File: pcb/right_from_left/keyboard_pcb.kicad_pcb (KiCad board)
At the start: 2 copper layers, 138.8 x 89.9 mm, 48 parts, among them J1 TRRS, J2 Conn_01x04_Male, K0 KEYSW, K1 KEYSW, K10 KEYSW, K11 KEYSW, K12 KEYSW, K13 KEYSW, K14 KEYSW, K15 KEYSW, K2 KEYSW, K20 KEYSW, K21 KEYSW, K22 KEYSW, K23 KEYSW, K24 KEYSW, K25 KEYSW, K3 KEYSW, K30 KEYSW, K31 KEYSW, K32 KEYSW, K4 KEYSW, K5 KEYSW, U1 PCF8574, U2 Pico

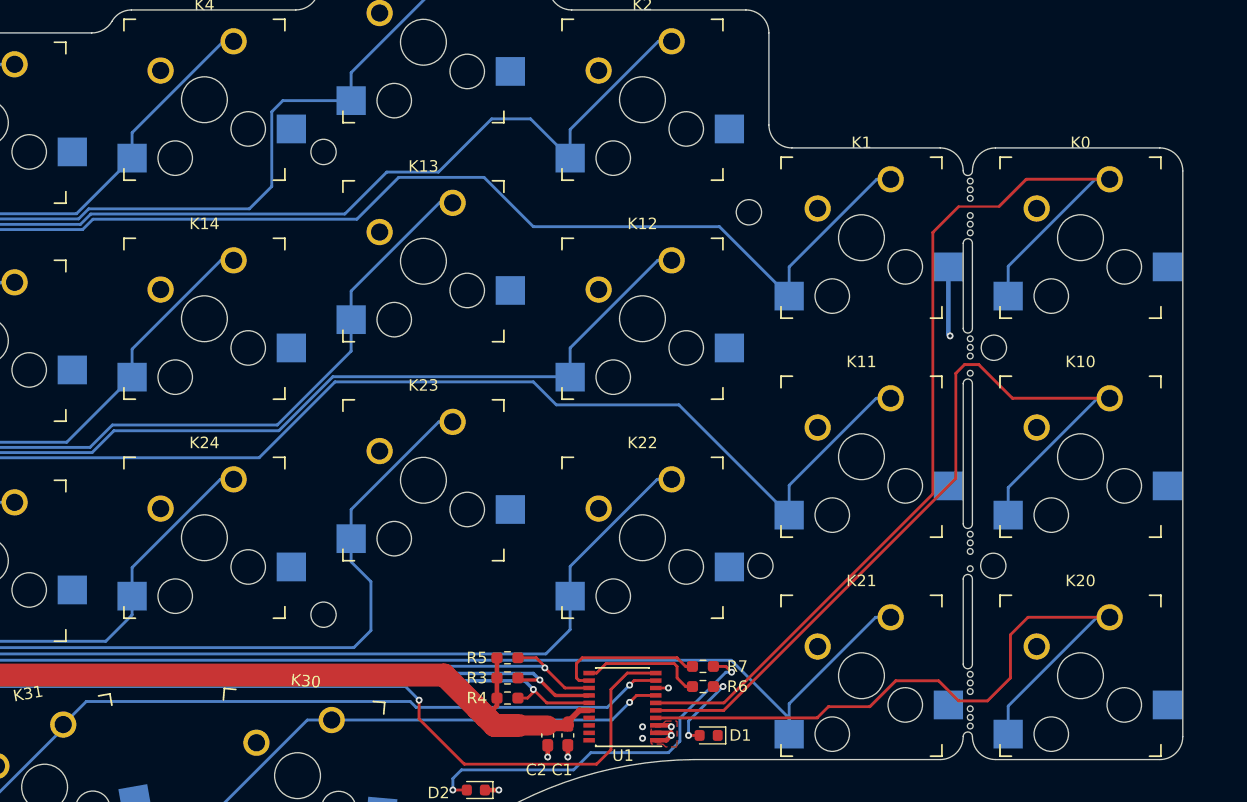
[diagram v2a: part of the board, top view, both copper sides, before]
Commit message: left keyboards routed
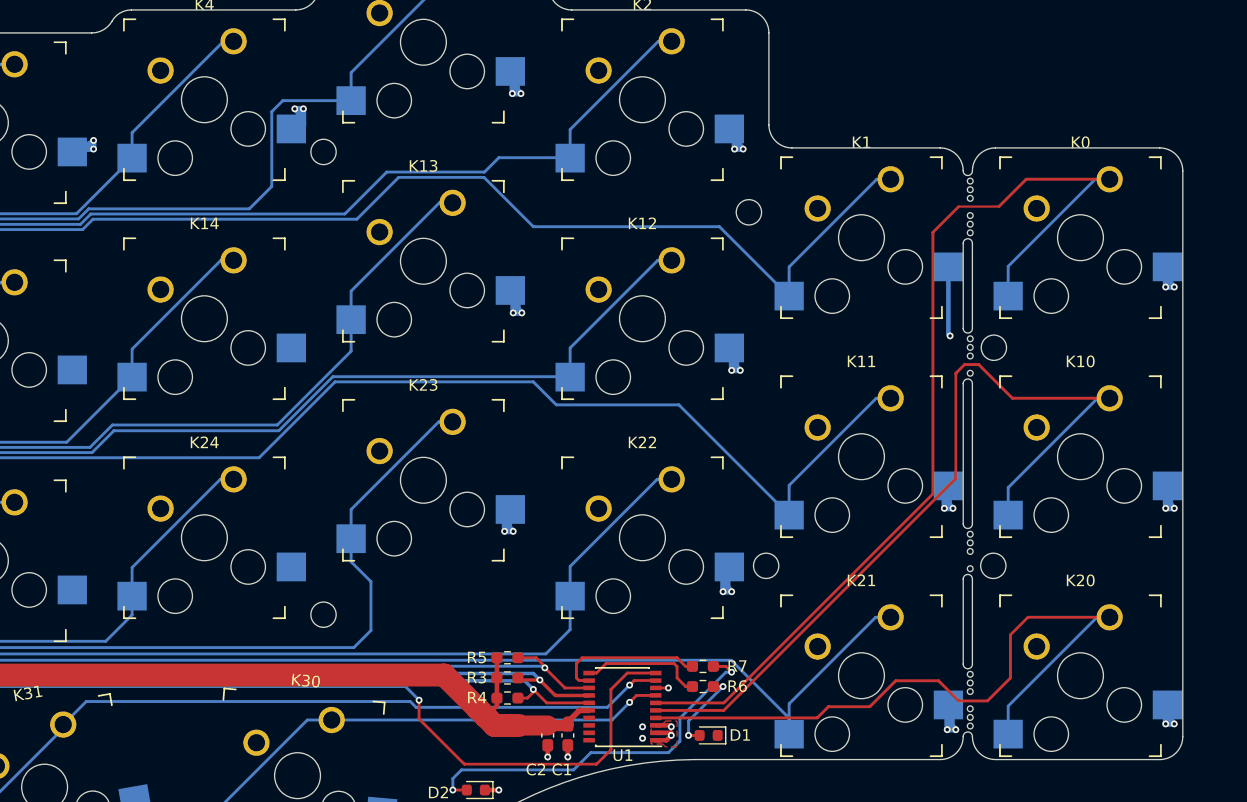
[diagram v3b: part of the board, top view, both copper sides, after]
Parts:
- moved H4 0.50 mm to (169.0, 96.8)
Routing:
- net GND: track 16.1 -> 71.6 mm, vias 10 -> 36
- net /k02: track 86.7 -> 83.9 mm
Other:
- board text added: "Right"

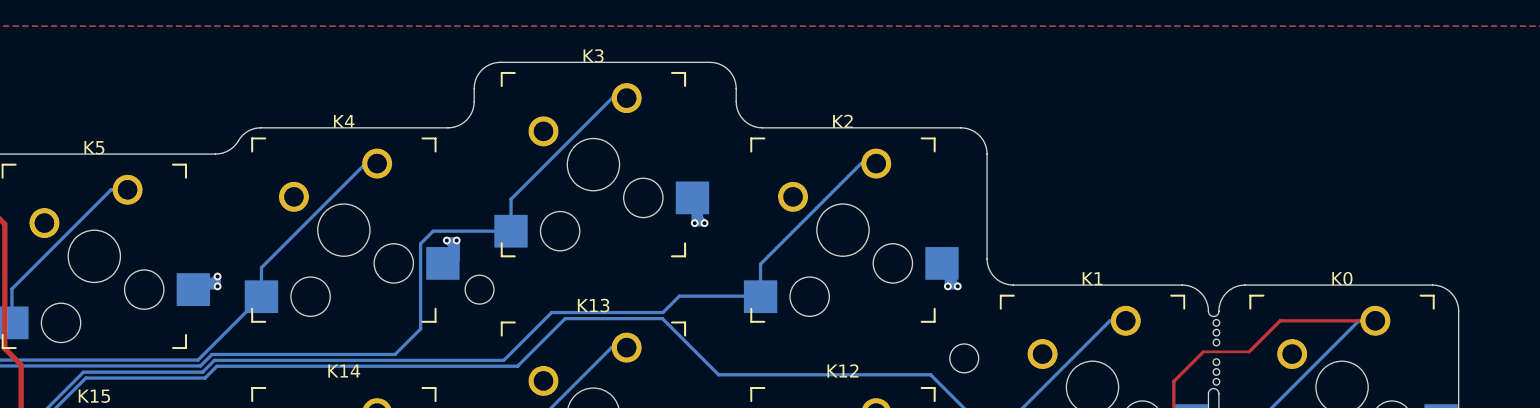
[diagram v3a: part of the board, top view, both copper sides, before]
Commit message: Left keyboard: Jumper to switch RX/TX direction removed in schematic and pcb.
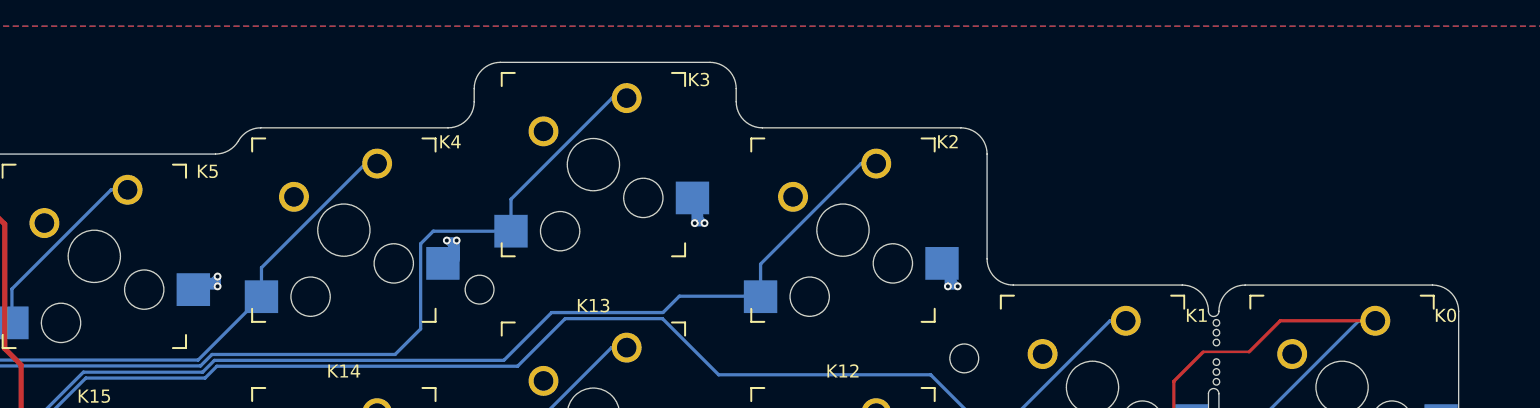
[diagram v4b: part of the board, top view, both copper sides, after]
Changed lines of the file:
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@@
         (effects (font (size 1 1) (thickness 0.15)))
     )
-    (fp_text value "KEYSW" (at 0 8.255) (layer "F.Fab")
+    (fp_text value "KEYSW" (at 4.46 -2.058) (layer "F.Fab")
         (effects (font (size 1 1) (thickness 0.15)))
     )
-    (fp_text user "${REFERENCE}" (at 3.81 8.255) (layer "B.SilkS")
+    (fp_text user "${REFERENCE}" (at 6.21 -7.558) (layer "B.SilkS")
         (effects (font (size 1 1) (thickness 0.15)) (justify mirror))
     )
-    (fp_text user "${VALUE}" (at 0 8.255) (layer "B.Fab")
+    (fp_text user "${VALUE}" (at 4.46 -2.058) (layer "B.Fab")
         (effects (font (size 1 1) (thickness 0.15)) (justify mirror))
     )
@@
     (property "Sheetname" "")
     (attr through_hole exclude_from_pos_files)
-    (fp_text reference "K2" (at 0 -8.255) (layer "F.SilkS")
+    (fp_text reference "K2" (at 8.01 -6.708) (layer "F.SilkS")
         (effects (font (size 1 1) (thickness 0.15)))
     )
@@
     (property "Sheetname" "")
     (attr through_hole exclude_from_pos_files)
-    (fp_text reference "K4" (at 0 -8.255) (layer "F.SilkS")
+    (fp_text reference "K4" (at 8.11 -6.708) (layer "F.SilkS")
         (effects (font (size 1 1) (thickness 0.15)))
     )
@@
         (effects (font (size 1 1) (thickness 0.15)))
     )
-    (fp_text value "KEYSW" (at 0 8.255 175) (layer "F.Fab")
+    (fp_text value "KEYSW" (at 9.974957 4.899268 175) (layer "F.Fab")
         (effects (font (size 1 1) (thickness 0.15)))
     )
@@
         (effects (font (size 1 1) (thickness 0.15)) (justify mirror))
     )
-    (fp_text user "${VALUE}" (at 0 8.255 175) (layer "B.Fab")
+    (fp_text user "${VALUE}" (at 9.974957 4.899268 175) (layer "B.Fab")
         (effects (font (size 1 1) (thickness 0.15)) (justify mirror))
     )
@@
     (property "Sheetname" "")
     (attr through_hole exclude_from_pos_files)
-    (fp_text reference "K1" (at 0 -8.255) (layer "F.SilkS")
+    (fp_text reference "K1" (at 7.96 -5.458) (layer "F.SilkS")
         (effects (font (size 1 1) (thickness 0.15)))
     )
@@
         (effects (font (size 1 1) (thickness 0.15)))
     )
-    (fp_text value "KEYSW" (at 0 8.255 25) (layer "F.Fab")
+    (fp_text value "KEYSW" (at 9.933865 7.114838 25) (layer "F.Fab")
         (effects (font (size 1 1) (thickness 0.15)))
     )
@@
         (effects (font (size 1 1) (thickness 0.15)) (justify mirror))
     )
-    (fp_text user "${VALUE}" (at 0 8.255 25) (layer "B.Fab")
+    (fp_text user "${VALUE}" (at 9.933865 7.114838 25) (layer "B.Fab")
         (effects (font (size 1 1) (thickness 0.15)) (justify mirror))
     )
@@
     (property "Sheetname" "")
     (attr through_hole)
-    (fp_text reference "K3" (at 0 -8.255) (layer "F.SilkS")
+    (fp_text reference "K3" (at 8.06 -6.458) (layer "F.SilkS")
         (effects (font (size 1 1) (thickness 0.15)))
     )
@@
     (property "Sheetname" "")
     (attr through_hole exclude_from_pos_files)
-    (fp_text reference "K5" (at 0 -8.255) (layer "F.SilkS")
+    (fp_text reference "K5" (at 8.66 -6.458) (layer "F.SilkS")
         (effects (font (size 1 1) (thickness 0.15)))
     )
@@
         (effects (font (size 1 1) (thickness 0.15)))
     )
-    (fp_text user "${REFERENCE}" (at 7.16 -1.558) (layer "B.SilkS")
+    (fp_text user "${REFERENCE}" (at 6.66 -8.308) (layer "B.SilkS")
         (effects (font (size 1 1) (thickness 0.15)) (justify mirror))
     )
@@
     (property "Sheetname" "")
     (attr through_hole exclude_from_pos_files)
-    (fp_text reference "K0" (at 0 -8.255) (layer "F.SilkS")
+    (fp_text reference "K0" (at 7.91 -5.458) (layer "F.SilkS")
         (effects (font (size 1 1) (thickness 0.15)))
     )
@@
         (effects (font (size 1 1) (thickness 0.15)))
     )
-    (fp_text value "KEYSW" (at 0 8.255 10) (layer "F.Fab")
+    (fp_text value "KEYSW" (at 9.988763 5.315282 10) (layer "F.Fab")
         (effects (font (size 1 1) (thickness 0.15)))
     )
@@
         (effects (font (size 1 1) (thickness 0.15)) (justify mirror))
     )
-    (fp_text user "${VALUE}" (at 0 8.255 10) (layer "B.Fab")
+    (fp_text user "${VALUE}" (at 9.988763 5.315282 10) (layer "B.Fab")
         (effects (font (size 1 1) (thickness 0.15)) (justify mirror))
     )

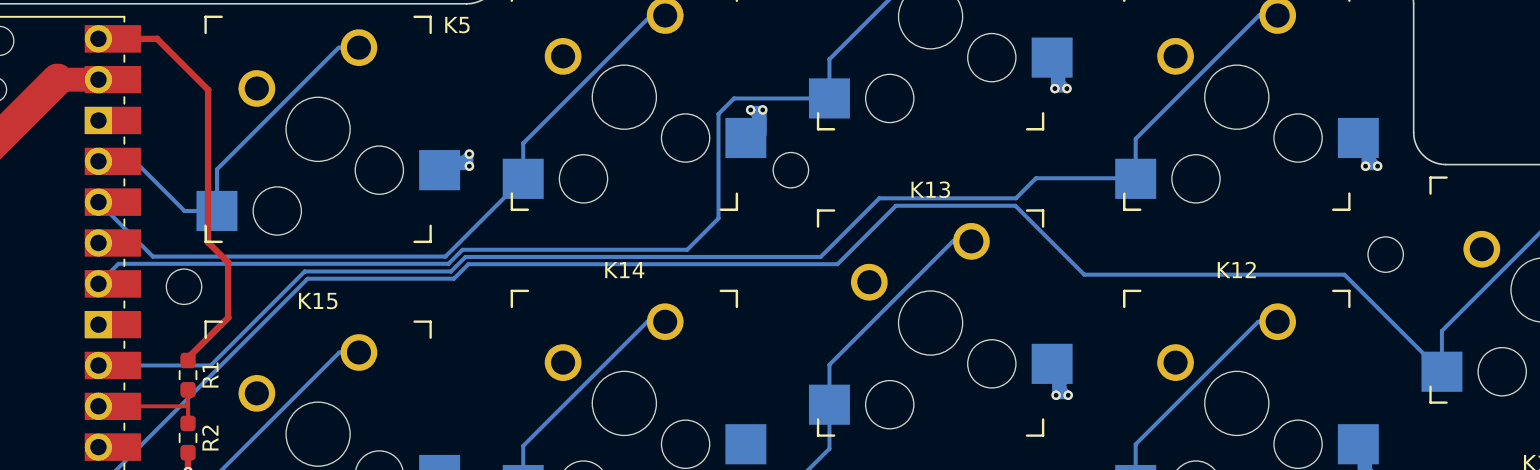
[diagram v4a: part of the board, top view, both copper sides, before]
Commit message: finetuning regarding BOM and part placement
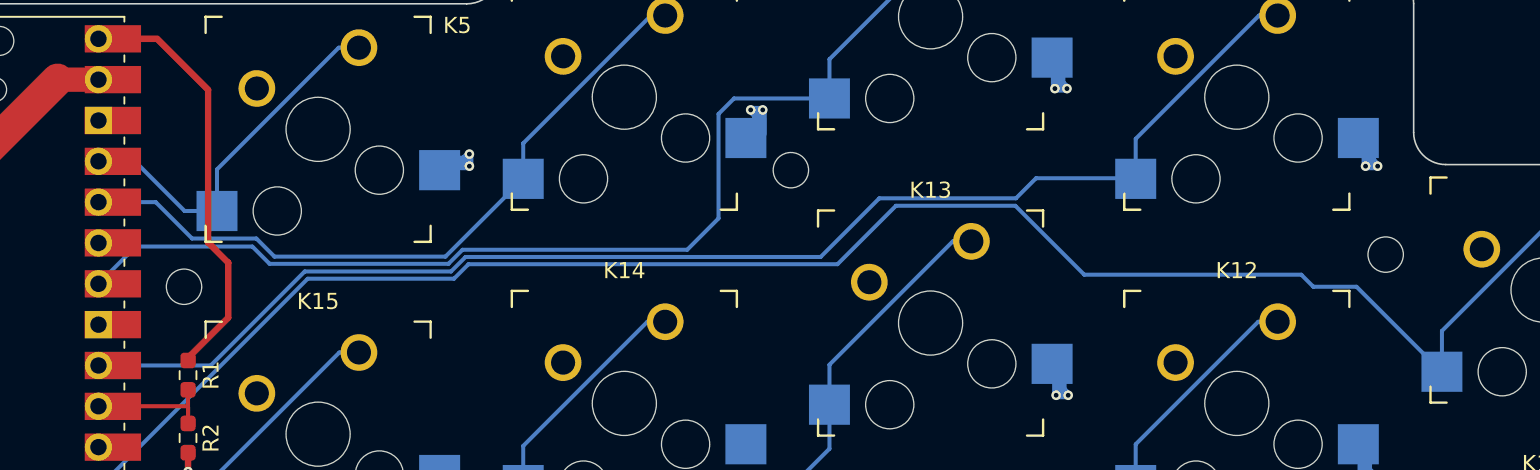
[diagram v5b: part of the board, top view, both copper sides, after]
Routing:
- net /k03: track 68.5 -> 69.4 mm
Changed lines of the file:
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@@
     (property "Sheetfile" "keyboard_pcb.kicad_sch")
     (property "Sheetname" "")
-    (attr through_hole exclude_from_pos_files)
+    (attr through_hole exclude_from_pos_files exclude_from_bom)
     (fp_text reference "J1" (at 0 14.2 90) (layer "Dwgs.User") hide
         (effects (font (size 1 1) (thickness 0.15)))
@@
   (segment (start 197.622 63.128) (end 198.88 63.128) (width 0.25) (layer "B.Cu") (net 2))
   (segment (start 190.05 70.7) (end 197.622 63.128) (width 0.25) (layer "B.Cu") (net 2))
+  (segment (start 100.4448 67.5) (end 109.54507 67.5) (width 0.25) (layer "B.Cu") (net 3))
   (segment (start 137.037 62.963) (end 144.463 62.963) (width 0.25) (layer "B.Cu") (net 3))
+  (segment (start 133.401497 66.598503) (end 137.037 62.963) (width 0.25) (layer "B.Cu") (net 3))
+  (segment (start 165.687 68) (end 170.975 73.288) (width 0.25) (layer "B.Cu") (net 3))
+  (segment (start 148.75 67.25) (end 162.25 67.25) (width 0.25) (layer "B.Cu") (net 3))
+  (segment (start 162.25 67.25) (end 163 68) (width 0.25) (layer "B.Cu") (net 3))
+  (segment (start 144.463 62.963) (end 148.75 67.25) (width 0.25) (layer "B.Cu") (net 3))
+  (segment (start 87.4268 80.518) (end 100.4448 67.5) (width 0.25) (layer "B.Cu") (net 3))
+  (segment (start 163 68) (end 165.687 68) (width 0.25) (layer "B.Cu") (net 3))
+  (segment (start 109.54507 67.5) (end 110.446567 66.598503) (width 0.25) (layer "B.Cu") (net 3))
+  (segment (start 171 70.75) (end 178.622 63.128) (width 0.25) (layer "B.Cu") (net 3))
+  (segment (start 170.975 73.288) (end 171 73.288) (width 0.25) (layer "B.Cu") (net 3))
   (segment (start 110.446567 66.598503) (end 133.401497 66.598503) (width 0.25) (layer "B.Cu") (net 3))
-  (segment (start 109.54507 67.5) (end 110.446567 66.598503) (width 0.25) (layer "B.Cu") (net 3))
-  (segment (start 148.75 67.25) (end 164.937 67.25) (width 0.25) (layer "B.Cu") (net 3))
-  (segment (start 170.975 73.288) (end 171 73.288) (width 0.25) (layer "B.Cu") (net 3))
-  (segment (start 100.4448 67.5) (end 109.54507 67.5) (width 0.25) (layer "B.Cu") (net 3))
-  (segment (start 87.4268 80.518) (end 100.4448 67.5) (width 0.25) (layer "B.Cu") (net 3))
-  (segment (start 144.463 62.963) (end 148.75 67.25) (width 0.25) (layer "B.Cu") (net 3))
-  (segment (start 133.401497 66.598503) (end 137.037 62.963) (width 0.25) (layer "B.Cu") (net 3))
-  (segment (start 164.937 67.25) (end 170.975 73.288) (width 0.25) (layer "B.Cu") (net 3))
-  (segment (start 171 70.75) (end 178.622 63.128) (width 0.25) (layer "B.Cu") (net 3))
   (segment (start 178.622 63.128) (end 179.83 63.128) (width 0.25) (layer "B.Cu") (net 3))
   (segment (start 171 73.288) (end 171 70.75) (width 0.25) (layer "B.Cu") (net 3))
@@
   (segment (start 144.5 62.5) (end 145.75 61.25) (width 0.25) (layer "B.Cu") (net 4))
   (segment (start 94.41111 72.898) (end 100.258611 67.050499) (width 0.25) (layer "B.Cu") (net 4))
-  (segment (start 124.050499 65.699501) (end 126 63.75) (width 0.25) (layer "B.Cu") (net 5))
-  (segment (start 109.19869 66.575) (end 110.074189 65.699501) (width 0.25) (layer "B.Cu") (net 5))
+  (segment (start 97 65.5) (end 89.7448 65.5) (width 0.25) (layer "B.Cu") (net 5))
+  (segment (start 126.962 56.288) (end 126 57.25) (width 0.25) (layer "B.Cu") (net 5))
+  (segment (start 89.7448 65.5) (end 87.4268 67.818) (width 0.25) (layer "B.Cu") (net 5))
+  (segment (start 98.075 66.575) (end 97 65.5) (width 0.25) (layer "B.Cu") (net 5))
+  (segment (start 109.19869 66.575) (end 98.075 66.575) (width 0.25) (layer "B.Cu") (net 5))
   (segment (start 132.9 53.85) (end 140.622 46.128) (width 0.25) (layer "B.Cu") (net 5))
-  (segment (start 88.6698 66.575) (end 109.19869 66.575) (width 0.25) (layer "B.Cu") (net 5))
-  (segment (start 126 57.25) (end 126.962 56.288) (width 0.25) (layer "B.Cu") (net 5))
-  (segment (start 126.962 56.288) (end 132.9 56.288) (width 0.25) (layer "B.Cu") (net 5))
-  (segment (start 126 63.75) (end 126 57.25) (width 0.25) (layer "B.Cu") (net 5))
+  (segment (start 126 63.75) (end 124.050499 65.699501) (width 0.25) (layer "B.Cu") (net 5))
+  (segment (start 110.074189 65.699501) (end 109.19869 66.575) (width 0.25) (layer "B.Cu") (net 5))
   (segment (start 132.9 56.288) (end 132.9 53.85) (width 0.25) (layer "B.Cu") (net 5))
-  (segment (start 110.074189 65.699501) (end 124.050499 65.699501) (width 0.25) (layer "B.Cu") (net 5))
-  (segment (start 87.4268 67.818) (end 88.6698 66.575) (width 0.25) (layer "B.Cu") (net 5))
+  (segment (start 132.9 56.288) (end 126.962 56.288) (width 0.25) (layer "B.Cu") (net 5))
+  (segment (start 124.050499 65.699501) (end 110.074189 65.699501) (width 0.25) (layer "B.Cu") (net 5))
   (segment (start 140.622 46.128) (end 141.73 46.128) (width 0.25) (layer "B.Cu") (net 5))
-  (segment (start 87.4268 62.738) (end 90.814299 66.125499) (width 0.25) (layer "B.Cu") (net 6))
+  (segment (start 126 57.25) (end 126 63.75) (width 0.25) (layer "B.Cu") (net 5))
+  (segment (start 109.012501 66.125499) (end 98.375499 66.125499) (width 0.25) (layer "B.Cu") (net 6))
+  (segment (start 93.25 65) (end 90.988 62.738) (width 0.25) (layer "B.Cu") (net 6))
+  (segment (start 98.375499 66.125499) (end 97.25 65) (width 0.25) (layer "B.Cu") (net 6))
   (segment (start 121.799159 51.128) (end 122.68 51.128) (width 0.25) (layer "B.Cu") (net 6))
   (segment (start 113.85 61.288) (end 113.85 59.077159) (width 0.25) (layer "B.Cu") (net 6))
+  (segment (start 97.25 65) (end 93.25 65) (width 0.25) (layer "B.Cu") (net 6))
+  (segment (start 113.85 61.288) (end 109.012501 66.125499) (width 0.25) (layer "B.Cu") (net 6))
+  (segment (start 90.988 62.738) (end 87.4268 62.738) (width 0.25) (layer "B.Cu") (net 6))
   (segment (start 113.85 59.077159) (end 121.799159 51.128) (width 0.25) (layer "B.Cu") (net 6))
-  (segment (start 90.814299 66.125499) (end 109.012501 66.125499) (width 0.25) (layer "B.Cu") (net 6))
-  (segment (start 109.012501 66.125499) (end 113.85 61.288) (width 0.25) (layer "B.Cu") (net 6))
   (segment (start 102.372 53.128) (end 103.63 53.128) (width 0.25) (layer "B.Cu") (net 7))
   (segment (start 92.788 63.288) (end 94.8 63.288) (width 0.25) (layer "B.Cu") (net 7))

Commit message: v1.0
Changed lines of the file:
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@@
   (gr_rect (start 68.707 62.611) (end 87.757 106.172)
     (stroke (width 0.2) (type solid)) (fill none) (layer "User.9"))
+  (gr_text "Right" (at 80.25 111.25) (layer "F.SilkS")
+    (effects (font (size 2 2) (thickness 0.3) bold) (justify left bottom))
+  )
   (gr_text "v1.0" (at 70 117.75) (layer "F.SilkS")
     (effects (font (size 1.5 1.5) (thickness 0.3) bold) (justify left bottom))
